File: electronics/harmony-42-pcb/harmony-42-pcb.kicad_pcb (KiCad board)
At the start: 2 copper layers, 0 parts

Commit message: Add keys
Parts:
- added D1: 1N4148WS, Project_Library:D_SOD-323F, F.Cu at (38.9, 71.0)
- added D2: 1N4148WS, Project_Library:D_SOD-323F, F.Cu at (57.6, 58.0)
- added D3: 1N4148WS, Project_Library:D_SOD-323F, F.Cu at (77.4, 55.5)
- added D4: 1N4148WS, Project_Library:D_SOD-323F, F.Cu at (95.6, 60.0)
- added D5: 1N4148WS, Project_Library:D_SOD-323F, F.Cu at (112.0, 63.0)
- added D6: 1N4148WS, Project_Library:D_SOD-323F, F.Cu at (128.9, 72.5)
- added SW1: ~, Project_Library:Hot_Swap_Socket_CPG151101S11, F.Cu at (38.7, 48.6)
- added SW2: ~, Project_Library:Hot_Swap_Socket_CPG151101S11, F.Cu at (57.8, 39.1)
- added SW3: ~, Project_Library:Hot_Swap_Socket_CPG151101S11, F.Cu at (78.2, 35.5)
- added SW4: ~, Project_Library:Hot_Swap_Socket_CPG151101S11, F.Cu at (98.5, 39.0)
- added SW5: ~, Project_Library:Hot_Swap_Socket_CPG151101S11, F.Cu at (118.2, 44.6)
- added SW6: ~, Project_Library:Hot_Swap_Socket_CPG151101S11, F.Cu at (137.1, 52.5)
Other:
- board outline added: 133.3 x 57.2 mm

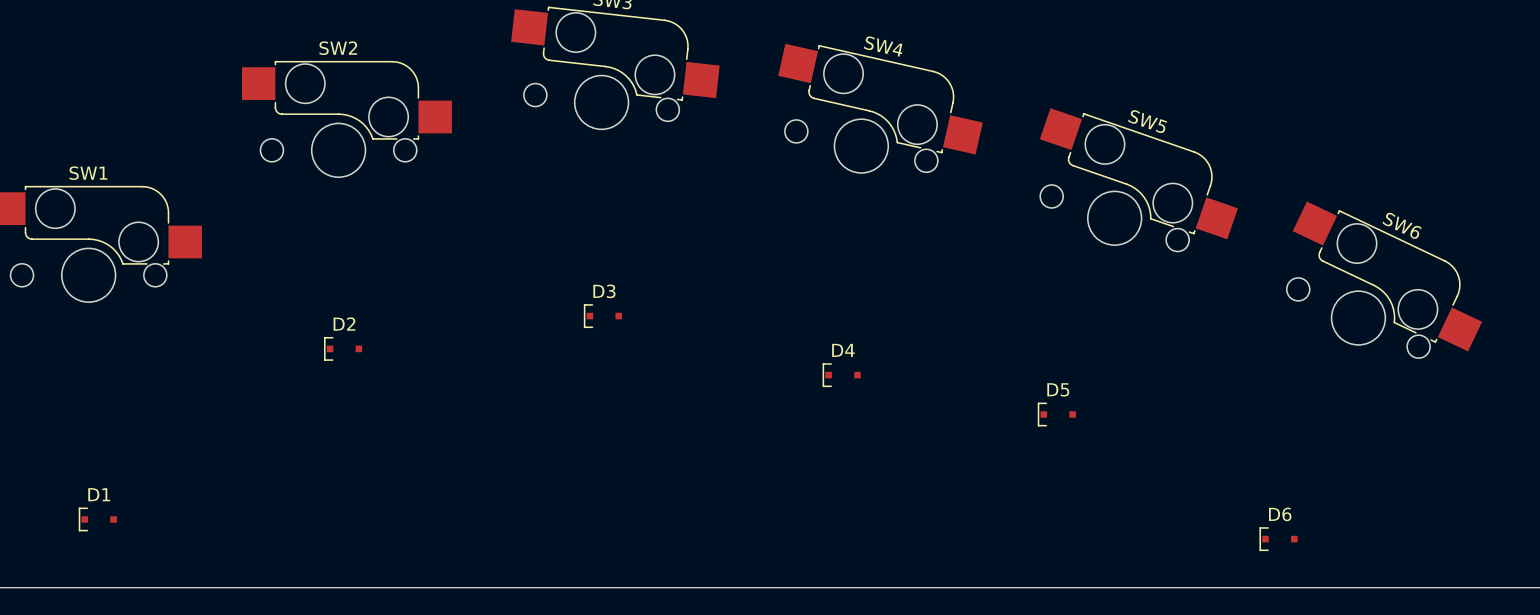
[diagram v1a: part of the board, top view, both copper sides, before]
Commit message: Add diodes
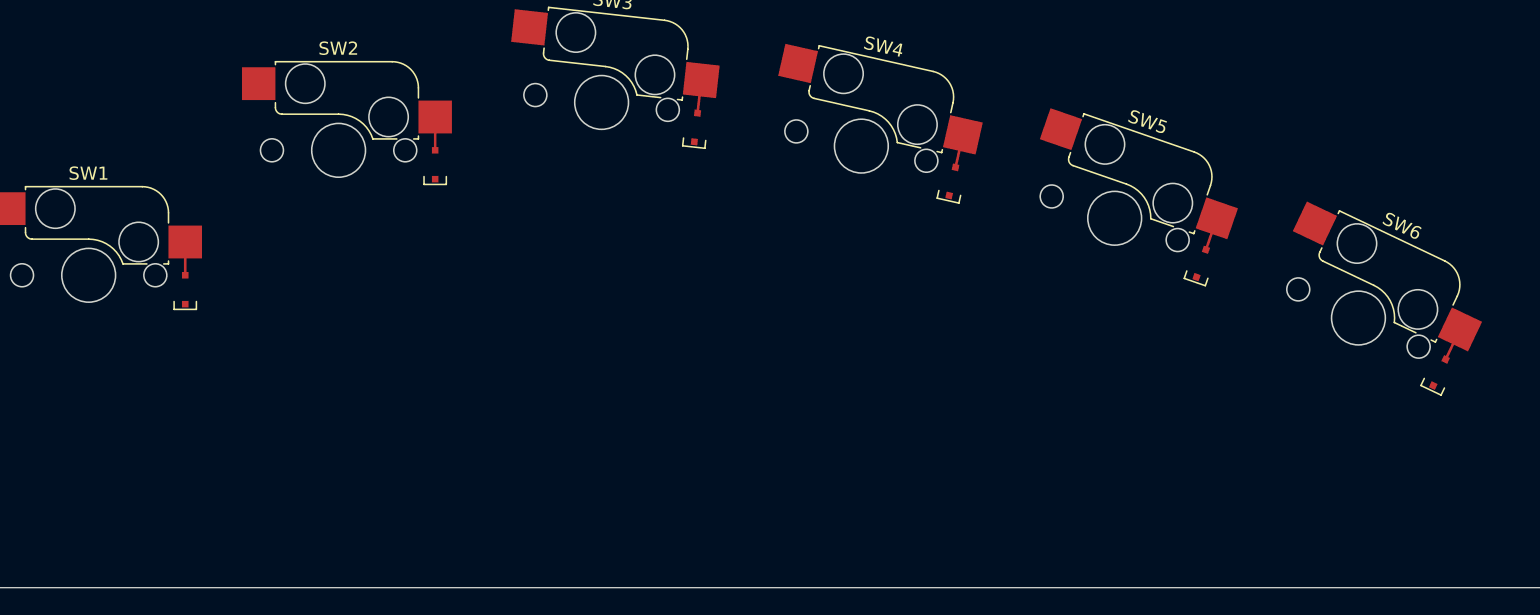
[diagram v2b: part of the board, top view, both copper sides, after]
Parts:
- moved D1 18.7 mm to (45.5, 53.5), turned to 90 degrees
- moved D6 17.6 mm to (141.1, 59.8), turned to 64.561 degrees
- moved D4 17.0 mm to (103.9, 45.2), turned to 77.28 degrees
- moved D3 16.0 mm to (84.4, 41.1), turned to 83.64 degrees
- moved D5 15.9 mm to (122.9, 51.5), turned to 70.921 degrees
- moved D2 15.6 mm to (64.5, 44.0), turned to 90 degrees
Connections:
- SW1 pad 1: Net-(D1-A) -> unconnected-(SW1-Pad1)
- SW1 pad 2: unconnected-(SW1-Pad2) -> Net-(D1-A)
- SW2 pad 1: Net-(D2-A) -> unconnected-(SW2-Pad1)
- SW2 pad 2: unconnected-(SW2-Pad2) -> Net-(D2-A)
- SW3 pad 1: Net-(D3-A) -> unconnected-(SW3-Pad1)
- SW3 pad 2: unconnected-(SW3-Pad2) -> Net-(D3-A)
- SW4 pad 1: Net-(D4-A) -> unconnected-(SW4-Pad1)
- SW4 pad 2: unconnected-(SW4-Pad2) -> Net-(D4-A)
- SW5 pad 1: Net-(D5-A) -> unconnected-(SW5-Pad1)
- SW5 pad 2: unconnected-(SW5-Pad2) -> Net-(D5-A)
- SW6 pad 1: Net-(D6-A) -> unconnected-(SW6-Pad1)
- SW6 pad 2: unconnected-(SW6-Pad2) -> Net-(D6-A)
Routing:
- net Net-(D5-A): track 0.00 -> 2.67 mm
- net Net-(D1-A): track 0.00 -> 2.54 mm
- net Net-(D2-A): track 0.00 -> 2.54 mm
- net Net-(D3-A): track 0.00 -> 2.54 mm
- net Net-(D6-A): track 0.00 -> 2.54 mm
- net Net-(D4-A): track 0.00 -> 2.54 mm

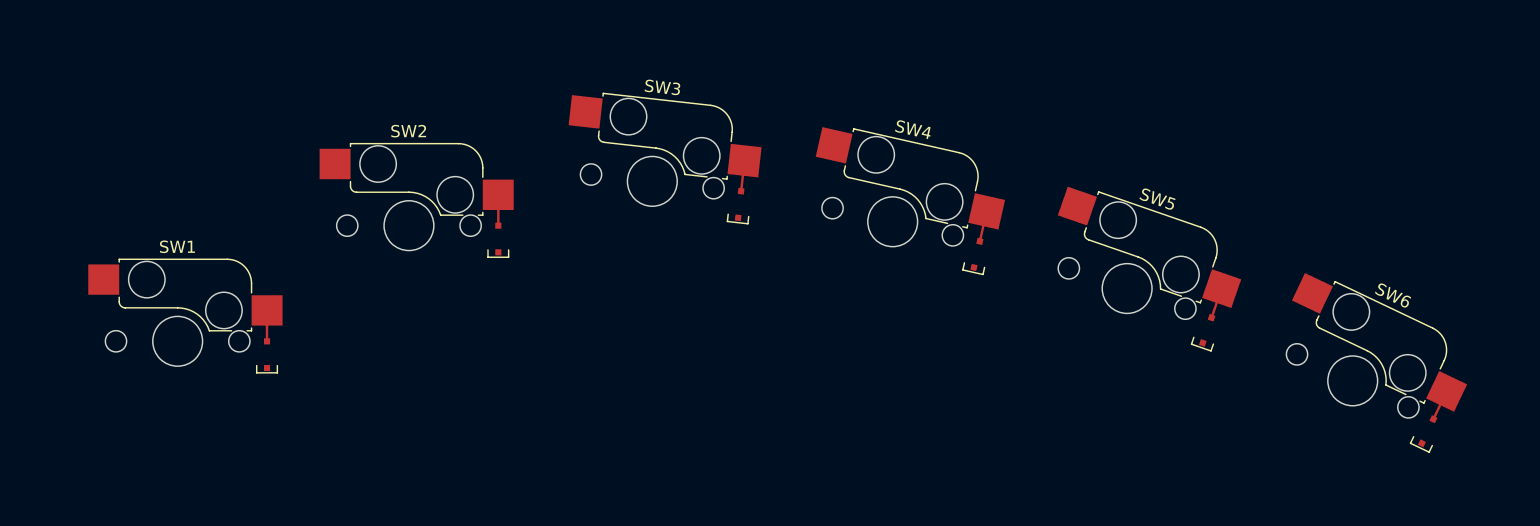
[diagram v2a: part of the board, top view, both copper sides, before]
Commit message: Fix mounting side of parts
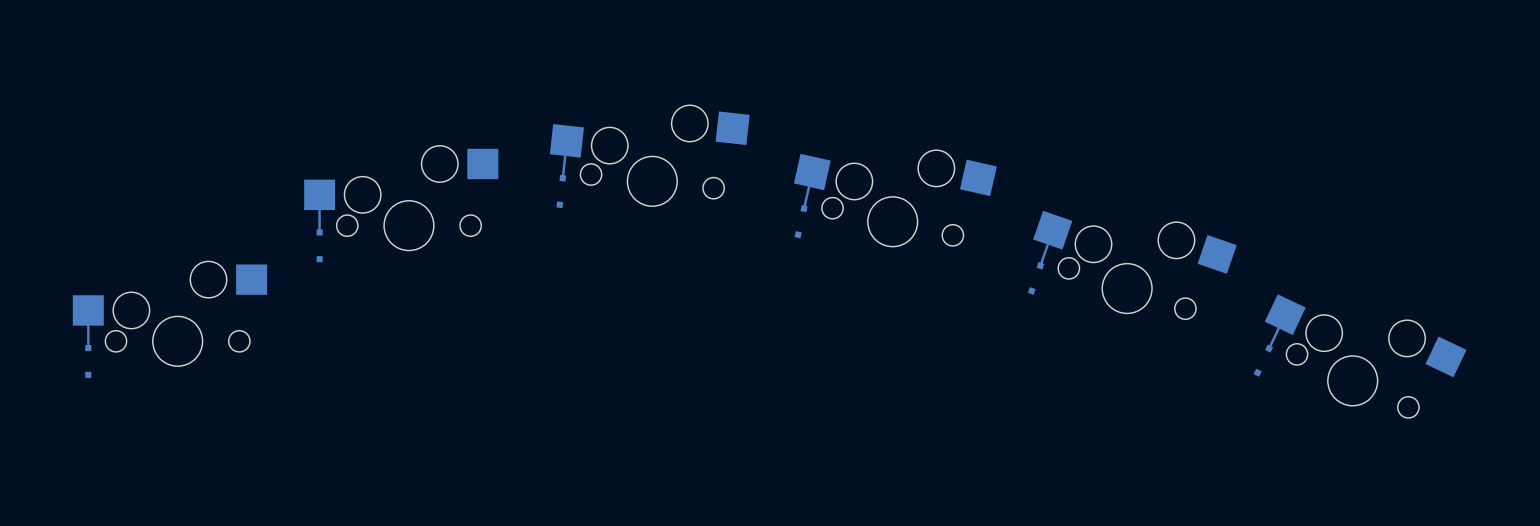
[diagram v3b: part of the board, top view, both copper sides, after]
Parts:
- D1, D2, D3, D4, D5, D6, SW1, SW2, SW3, SW4, SW5, SW6: moved to B.Cu
- moved D6 14.7 mm to (127.5, 54.0)
- moved D5 14.7 mm to (108.8, 47.2)
- moved D3 14.7 mm to (69.7, 40.0)
- moved D2 14.7 mm to (49.8, 44.5)
- moved D1 14.7 mm to (30.7, 54.0)
- moved D4 14.7 mm to (89.5, 42.5)
- moved SW4 1.27 mm to (97.2, 38.7), turned to -12.719 degrees
- moved SW6 1.27 mm to (135.9, 51.9), turned to -25.438 degrees
- moved SW1 1.27 mm to (37.5, 48.6), turned to 0 degrees
- moved SW2 1.27 mm to (56.5, 39.1), turned to 0 degrees
- moved SW5 1.27 mm to (117.0, 44.2), turned to -19.079 degrees
- moved SW3 1.27 mm to (77.0, 35.4), turned to -6.36 degrees
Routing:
- net Net-(D4-A): track 2.54 -> 3.10 mm
- net Net-(D3-A): track 2.54 -> 3.10 mm
- net Net-(D2-A): track 2.54 -> 3.10 mm
- net Net-(D1-A): track 2.54 -> 3.10 mm
- net Net-(D6-A): track 2.54 -> 3.10 mm

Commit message: Add keys
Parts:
- added D10: 1N4148WS, Project_Library:D_SOD-323F, F.Cu at (248.6, 41.8)
- added D11: 1N4148WS, Project_Library:D_SOD-323F, F.Cu at (248.6, 44.8)
- added D12: 1N4148WS, Project_Library:D_SOD-323F, F.Cu at (248.6, 47.7)
- added D13: 1N4148WS, Project_Library:D_SOD-323F, B.Cu at (30.7, 73.1)
- added D14: 1N4148WS, Project_Library:D_SOD-323F, B.Cu at (49.8, 63.6)
- added D15: 1N4148WS, Project_Library:D_SOD-323F, B.Cu at (69.8, 59.1)
- added D16: 1N4148WS, Project_Library:D_SOD-323F, B.Cu at (89.6, 62.0)
- added D17: 1N4148WS, Project_Library:D_SOD-323F, B.Cu at (108.9, 67.2)
- added D18: 1N4148WS, Project_Library:D_SOD-323F, B.Cu at (127.4, 74.9)
- added D19: 1N4148WS, Project_Library:D_SOD-323F, F.Cu at (252.9, 47.7)
- added D20: 1N4148WS, Project_Library:D_SOD-323F, F.Cu at (252.9, 50.7)
- added D21: 1N4148WS, Project_Library:D_SOD-323F, F.Cu at (257.1, 33.0)
- added D22: 1N4148WS, Project_Library:D_SOD-323F, F.Cu at (257.1, 35.9)
- added D23: 1N4148WS, Project_Library:D_SOD-323F, F.Cu at (257.1, 38.9)
- added D24: 1N4148WS, Project_Library:D_SOD-323F, F.Cu at (257.1, 41.8)
- added D7: 1N4148WS, Project_Library:D_SOD-323F, F.Cu at (248.6, 33.0)
- added D8: 1N4148WS, Project_Library:D_SOD-323F, F.Cu at (248.6, 35.9)
- added D9: 1N4148WS, Project_Library:D_SOD-323F, F.Cu at (248.6, 38.9)
- added SW10: ~, Project_Library:Hot_Swap_Socket_CPG151101S11, F.Cu at (195.4, 105.9)
- added SW11: ~, Project_Library:Hot_Swap_Socket_CPG151101S11, F.Cu at (195.4, 126.1)
- added SW12: ~, Project_Library:Hot_Swap_Socket_CPG151101S11, F.Cu at (195.4, 146.2)
- added SW13: ~, Project_Library:Hot_Swap_Socket_CPG151101S11, B.Cu at (37.5, 67.6)
- added SW14: ~, Project_Library:Hot_Swap_Socket_CPG151101S11, B.Cu at (56.5, 58.1)
- added SW15: ~, Project_Library:Hot_Swap_Socket_CPG151101S11, B.Cu at (77.2, 54.6)
- added SW16: ~, Project_Library:Hot_Swap_Socket_CPG151101S11, B.Cu at (97.5, 58.3)
- added SW17: ~, Project_Library:Hot_Swap_Socket_CPG151101S11, B.Cu at (117.2, 64.6)
- added SW18: ~, Project_Library:Hot_Swap_Socket_CPG151101S11, B.Cu at (136.0, 73.3)
- added SW19: ~, Project_Library:Hot_Swap_Socket_CPG151101S11, F.Cu at (235.8, 45.4)
- added SW20: ~, Project_Library:Hot_Swap_Socket_CPG151101S11, F.Cu at (235.8, 65.5)
- added SW21: ~, Project_Library:Hot_Swap_Socket_CPG151101S11, F.Cu at (235.8, 85.7)
- added SW22: ~, Project_Library:Hot_Swap_Socket_CPG151101S11, F.Cu at (235.8, 105.9)
- added SW23: ~, Project_Library:Hot_Swap_Socket_CPG151101S11, F.Cu at (235.8, 126.1)
- added SW24: ~, Project_Library:Hot_Swap_Socket_CPG151101S11, F.Cu at (235.8, 146.2)
- added SW7: ~, Project_Library:Hot_Swap_Socket_CPG151101S11, F.Cu at (195.4, 45.4)
- added SW8: ~, Project_Library:Hot_Swap_Socket_CPG151101S11, F.Cu at (195.4, 65.5)
- added SW9: ~, Project_Library:Hot_Swap_Socket_CPG151101S11, F.Cu at (195.4, 85.7)
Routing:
- net Net-(D13-A): track 0.00 -> 3.10 mm
- net Net-(D14-A): track 0.00 -> 3.10 mm
- net Net-(D16-A): track 0.00 -> 3.10 mm
- net Net-(D17-A): track 0.00 -> 3.10 mm
- net Net-(D18-A): track 0.00 -> 3.10 mm
- net Net-(D15-A): track 0.00 -> 3.10 mm
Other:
- board size 133.3 x 57.2 mm -> 133.3 x 95.2 mm

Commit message: Add keys
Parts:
- added D25: 1N4148WS, Project_Library:D_SOD-323F, B.Cu at (30.7, 92.1)
- added D26: 1N4148WS, Project_Library:D_SOD-323F, B.Cu at (49.8, 82.6)
- added D27: 1N4148WS, Project_Library:D_SOD-323F, B.Cu at (69.9, 78.2)
- added D28: 1N4148WS, Project_Library:D_SOD-323F, B.Cu at (89.8, 81.5)
- added D29: 1N4148WS, Project_Library:D_SOD-323F, B.Cu at (109.0, 87.5)
- added D30: 1N4148WS, Project_Library:D_SOD-323F, B.Cu at (127.2, 96.2)
- added D31: 1N4148WS, Project_Library:D_SOD-323F, F.Cu at (364.6, 49.7)
- added D32: 1N4148WS, Project_Library:D_SOD-323F, F.Cu at (368.9, 32.0)
- added D33: 1N4148WS, Project_Library:D_SOD-323F, F.Cu at (368.9, 34.9)
- added D34: 1N4148WS, Project_Library:D_SOD-323F, F.Cu at (368.9, 37.9)
- added D35: 1N4148WS, Project_Library:D_SOD-323F, F.Cu at (368.9, 40.8)
- added D36: 1N4148WS, Project_Library:D_SOD-323F, F.Cu at (368.9, 43.8)
- added D37: 1N4148WS, Project_Library:D_SOD-323F, B.Cu at (126.8, 118.4)
- added D38: 1N4148WS, Project_Library:D_SOD-323F, B.Cu at (109.1, 108.3)
- added D39: 1N4148WS, Project_Library:D_SOD-323F, B.Cu at (90.1, 101.2)
- added D40: 1N4148WS, Project_Library:D_SOD-323F, F.Cu at (373.1, 34.9)
- added D41: 1N4148WS, Project_Library:D_SOD-323F, F.Cu at (373.1, 37.9)
- added D42: 1N4148WS, Project_Library:D_SOD-323F, F.Cu at (373.1, 40.8)
- added SW25: ~, Project_Library:Hot_Swap_Socket_CPG151101S11, B.Cu at (37.5, 86.7)
- added SW26: ~, Project_Library:Hot_Swap_Socket_CPG151101S11, B.Cu at (56.5, 77.2)
- added SW27: ~, Project_Library:Hot_Swap_Socket_CPG151101S11, B.Cu at (77.4, 73.8)
- added SW28: ~, Project_Library:Hot_Swap_Socket_CPG151101S11, B.Cu at (97.8, 78.1)
- added SW29: ~, Project_Library:Hot_Swap_Socket_CPG151101S11, B.Cu at (117.4, 85.3)
- added SW30: ~, Project_Library:Hot_Swap_Socket_CPG151101S11, B.Cu at (135.8, 95.3)
- added SW31: ~, Project_Library:Hot_Swap_Socket_CPG151101S11, F.Cu at (331.6, 44.4)
- added SW32: ~, Project_Library:Hot_Swap_Socket_CPG151101S11, F.Cu at (331.6, 64.5)
- added SW33: ~, Project_Library:Hot_Swap_Socket_CPG151101S11, F.Cu at (331.6, 84.7)
- added SW34: ~, Project_Library:Hot_Swap_Socket_CPG151101S11, F.Cu at (331.6, 104.9)
- added SW35: ~, Project_Library:Hot_Swap_Socket_CPG151101S11, F.Cu at (331.6, 125.1)
- added SW36: ~, Project_Library:Hot_Swap_Socket_CPG151101S11, F.Cu at (331.6, 145.2)
- added SW37: ~, Project_Library:Hot_Swap_Socket_CPG151101S11, B.Cu at (135.4, 118.3)
- added SW38: ~, Project_Library:Hot_Swap_Socket_CPG151101S11, B.Cu at (117.7, 106.7)
- added SW39: ~, Project_Library:Hot_Swap_Socket_CPG151101S11, B.Cu at (98.2, 98.2)
- added SW40: ~, Project_Library:Hot_Swap_Socket_CPG151101S11, F.Cu at (351.8, 104.9)
- added SW41: ~, Project_Library:Hot_Swap_Socket_CPG151101S11, F.Cu at (351.8, 125.1)
- added SW42: ~, Project_Library:Hot_Swap_Socket_CPG151101S11, F.Cu at (351.8, 145.2)
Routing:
- net Net-(D26-A): track 0.00 -> 3.10 mm
- net Net-(D25-A): track 0.00 -> 3.10 mm
- net Net-(D28-A): track 0.00 -> 3.10 mm
- net Net-(D27-A): track 0.00 -> 3.10 mm
- net Net-(D39-A): track 0.00 -> 3.10 mm
- net Net-(D37-A): track 0.00 -> 3.10 mm
- net Net-(D30-A): track 0.00 -> 3.10 mm
- net Net-(D38-A): track 0.00 -> 3.10 mm
- net Net-(D29-A): track 0.00 -> 3.10 mm
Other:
- board size 133.3 x 95.2 mm -> 133.3 x 133.3 mm

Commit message: Move diodes
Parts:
- D1, D13, D14, D15, D16, D17, D18, D2, D25, D26, D27, D28, D29, D3, D30, D37, D38, D39, D4, D5, D6, SW1, SW13, SW14, SW15, SW16, SW17, SW18, SW2, SW25, SW26, SW27, SW28, SW29, SW3, SW30, SW37, SW38, SW39, SW4, SW5, SW6: moved to F.Cu
- moved D36 326.0 mm to (45.5, 84.9), turned to -90 degrees
- moved D35 306.3 mm to (64.5, 75.4), turned to -90 degrees
- moved SW36 298.7 mm to (38.7, 86.7), turned to 180 degrees
- moved D34 285.5 mm to (85.5, 73.2), turned to -98.171 degrees
- moved SW35 278.0 mm to (57.8, 77.2), turned to 180 degrees
- moved D42 273.1 mm to (106.3, 99.2), turned to -109.054 degrees
- moved D33 266.5 mm to (106.0, 78.7), turned to -106.342 degrees
- moved D1 262.5 mm to (293.1, 46.8), turned to -90 degrees
- moved D13 262.5 mm to (293.1, 65.9), turned to -90 degrees
- moved D25 262.5 mm to (293.1, 84.9), turned to -90 degrees
- moved D41 257.6 mm to (125.5, 109.0), turned to -118.581 degrees
- moved SW42 256.6 mm to (99.4, 98.6), turned to 160.946 degrees
- moved SW34 254.9 mm to (78.6, 74.0), turned to 171.829 degrees
- moved D32 249.6 mm to (125.4, 87.1), turned to -114.513 degrees
- moved SW1 248.9 mm to (286.4, 48.6), turned to 180 degrees
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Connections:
- SW1 pad 1: unconnected-(SW1-Pad1) -> Net-(SW1-Pad1)
- SW10 pad 1: unconnected-(SW10-Pad1) -> Net-(SW10-Pad1)
- SW11 pad 1: unconnected-(SW11-Pad1) -> Net-(SW11-Pad1)
- SW12 pad 1: unconnected-(SW12-Pad1) -> Net-(SW12-Pad1)
- SW13 pad 1: unconnected-(SW13-Pad1) -> Net-(SW1-Pad1)
- SW14 pad 1: unconnected-(SW14-Pad1) -> Net-(SW14-Pad1)
- SW15 pad 1: unconnected-(SW15-Pad1) -> Net-(SW15-Pad1)
- SW16 pad 1: unconnected-(SW16-Pad1) -> Net-(SW16-Pad1)
- SW17 pad 1: unconnected-(SW17-Pad1) -> Net-(SW17-Pad1)
- SW18 pad 1: unconnected-(SW18-Pad1) -> Net-(SW18-Pad1)
- SW19 pad 1: unconnected-(SW19-Pad1) -> Net-(SW19-Pad1)
- SW2 pad 1: unconnected-(SW2-Pad1) -> Net-(SW14-Pad1)
- SW20 pad 1: unconnected-(SW20-Pad1) -> Net-(SW20-Pad1)
- SW21 pad 1: unconnected-(SW21-Pad1) -> Net-(SW21-Pad1)
- SW22 pad 1: unconnected-(SW22-Pad1) -> Net-(SW10-Pad1)
- SW23 pad 1: unconnected-(SW23-Pad1) -> Net-(SW11-Pad1)
- SW24 pad 1: unconnected-(SW24-Pad1) -> Net-(SW12-Pad1)
- SW25 pad 1: unconnected-(SW25-Pad1) -> Net-(SW1-Pad1)
- SW26 pad 1: unconnected-(SW26-Pad1) -> Net-(SW14-Pad1)
- SW27 pad 1: unconnected-(SW27-Pad1) -> Net-(SW15-Pad1)
- SW28 pad 1: unconnected-(SW28-Pad1) -> Net-(SW16-Pad1)
- SW29 pad 1: unconnected-(SW29-Pad1) -> Net-(SW17-Pad1)
- SW3 pad 1: unconnected-(SW3-Pad1) -> Net-(SW15-Pad1)
- SW30 pad 1: unconnected-(SW30-Pad1) -> Net-(SW18-Pad1)
- SW31 pad 1: unconnected-(SW31-Pad1) -> Net-(SW19-Pad1)
- SW32 pad 1: unconnected-(SW32-Pad1) -> Net-(SW20-Pad1)
- SW33 pad 1: unconnected-(SW33-Pad1) -> Net-(SW21-Pad1)
- SW34 pad 1: unconnected-(SW34-Pad1) -> Net-(SW10-Pad1)
- SW35 pad 1: unconnected-(SW35-Pad1) -> Net-(SW11-Pad1)
- SW36 pad 1: unconnected-(SW36-Pad1) -> Net-(SW12-Pad1)
- SW37 pad 1: unconnected-(SW37-Pad1) -> Net-(SW16-Pad1)
- SW38 pad 1: unconnected-(SW38-Pad1) -> Net-(SW17-Pad1)
- SW39 pad 1: unconnected-(SW39-Pad1) -> Net-(SW18-Pad1)
- SW4 pad 1: unconnected-(SW4-Pad1) -> Net-(SW16-Pad1)
- SW40 pad 1: unconnected-(SW40-Pad1) -> Net-(SW19-Pad1)
- SW41 pad 1: unconnected-(SW41-Pad1) -> Net-(SW20-Pad1)
- SW42 pad 1: unconnected-(SW42-Pad1) -> Net-(SW21-Pad1)
- SW5 pad 1: unconnected-(SW5-Pad1) -> Net-(SW17-Pad1)
- SW6 pad 1: unconnected-(SW6-Pad1) -> Net-(SW18-Pad1)
- SW7 pad 1: unconnected-(SW7-Pad1) -> Net-(SW19-Pad1)
- SW8 pad 1: unconnected-(SW8-Pad1) -> Net-(SW20-Pad1)
- SW9 pad 1: unconnected-(SW9-Pad1) -> Net-(SW21-Pad1)
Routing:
- net Net-(SW12-Pad1): track 0.00 -> 38.1 mm
- net Net-(D36-A): track 0.00 -> 1.90 mm
- net Net-(D35-A): track 0.00 -> 1.90 mm
- net Net-(D23-A): track 0.00 -> 1.90 mm
- net Net-(D12-A): track 0.00 -> 1.90 mm
- net Net-(D11-A): track 0.00 -> 1.90 mm
- net Net-(D24-A): track 0.00 -> 1.90 mm
- net Net-(D34-A): track 0.00 -> 1.90 mm
- net Net-(D22-A): track 0.00 -> 1.90 mm
- net Net-(D32-A): track 0.00 -> 1.90 mm
- net Net-(D42-A): track 0.00 -> 1.90 mm
- net Net-(D33-A): track 0.00 -> 1.90 mm
- net Net-(D21-A): track 0.00 -> 1.90 mm
- net Net-(D40-A): track 0.00 -> 1.90 mm
- net Net-(D20-A): track 0.00 -> 1.90 mm
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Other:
- board size 133.3 x 133.3 mm -> 285.8 x 133.3 mm

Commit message: Route some sw
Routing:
- net Net-(SW12-Pad1): track 38.1 -> 0.00 mm
- net Net-(SW10-Pad1): track 0.00 -> 2.40 mm, vias 0 -> 4
- net Net-(SW11-Pad1): track 0.00 -> 1.20 mm, vias 0 -> 2
